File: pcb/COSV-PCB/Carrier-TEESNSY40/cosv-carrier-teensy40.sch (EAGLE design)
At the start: 25 parts, among them X1 057-006-1, X3 22-23-2031, X4 22-23-2031, X5 22-23-2031, X6 22-23-2031, X7 22-23-2031

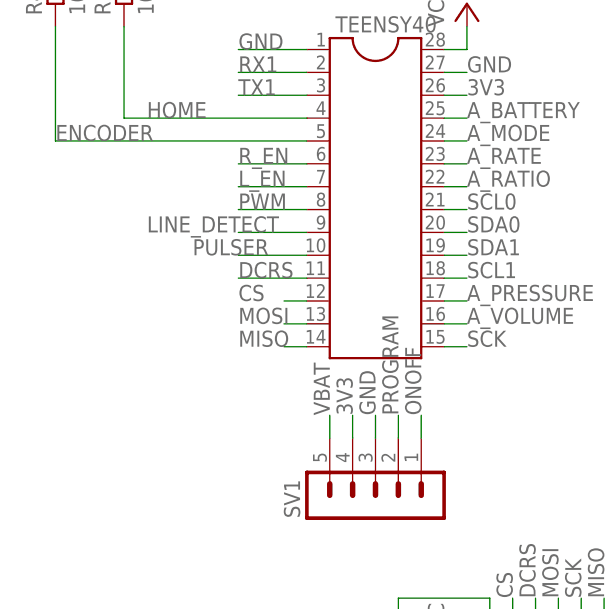
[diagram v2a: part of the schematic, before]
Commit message: Add Line Power Detect input and Watchdog Pulse output for alarm subsystem
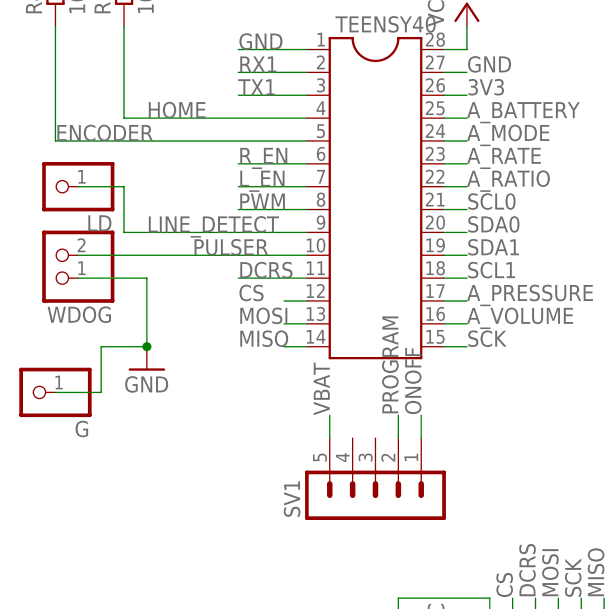
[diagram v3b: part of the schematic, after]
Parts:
- added G, LD: (no value), pinhead-2:PINHD-1X01_2.54-S
- added WDOG: (no value), pinhead:PINHD-1X2
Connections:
- net 3V3: no longer SV1.4
- net GND: now also G.1, WDOG.1; no longer SV1.3
- net LINE_DETECT: now also LD.1
- net PULSER: now also WDOG.2
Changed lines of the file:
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@@
 <grid distance="0.1" unitdist="inch" unit="inch" style="lines" multiple="1" display="no" altdistance="0.01" altunitdist="inch" altunit="inch"/>
 <layers>
-<layer number="1" name="Top" color="4" fill="1" visible="no" active="no"/>
-<layer number="16" name="Bottom" color="1" fill="1" visible="no" active="no"/>
-<layer number="17" name="Pads" color="2" fill="1" visible="no" active="no"/>
-<layer number="18" name="Vias" color="2" fill="1" visible="no" active="no"/>
-<layer number="19" name="Unrouted" color="6" fill="1" visible="no" active="no"/>
-<layer number="20" name="Dimension" color="15" fill="1" visible="no" active="no"/>
-<layer number="21" name="tPlace" color="7" fill="1" visible="no" active="no"/>
-<layer number="22" name="bPlace" color="7" fill="1" visible="no" active="no"/>
-<layer number="23" name="tOrigins" color="15" fill="1" visible="no" active="no"/>
-<layer number="24" name="bOrigins" color="15" fill="1" visible="no" active="no"/>
-<layer number="25" name="tNames" color="7" fill="1" visible="no" active="no"/>
-<layer number="26" name="bNames" color="7" fill="1" visible="no" active="no"/>
-<layer number="27" name="tValues" color="7" fill="1" visible="no" active="no"/>
-<layer number="28" name="bValues" color="7" fill="1" visible="no" active="no"/>
+<layer number="1" name="Top" color="4" fill="1" visible="yes" active="no"/>
+<layer number="16" name="Bottom" color="1" fill="1" visible="yes" active="no"/>
+<layer number="17" name="Pads" color="2" fill="1" visible="yes" active="no"/>
+<layer number="18" name="Vias" color="2" fill="1" visible="yes" active="no"/>
+<layer number="19" name="Unrouted" color="6" fill="1" visible="yes" active="no"/>
+<layer number="20" name="Dimension" color="15" fill="1" visible="yes" active="no"/>
+<layer number="21" name="tPlace" color="7" fill="1" visible="yes" active="no"/>
+<layer number="22" name="bPlace" color="7" fill="1" visible="yes" active="no"/>
+<layer number="23" name="tOrigins" color="15" fill="1" visible="yes" active="no"/>
+<layer number="24" name="bOrigins" color="15" fill="1" visible="yes" active="no"/>
+<layer number="25" name="tNames" color="7" fill="1" visible="yes" active="no"/>
+<layer number="26" name="bNames" color="7" fill="1" visible="yes" active="no"/>
+<layer number="27" name="tValues" color="7" fill="1" visible="yes" active="no"/>
+<layer number="28" name="bValues" color="7" fill="1" visible="yes" active="no"/>
 <layer number="29" name="tStop" color="7" fill="3" visible="no" active="no"/>
 <layer number="30" name="bStop" color="7" fill="6" visible="no" active="no"/>
@@
 <layer number="35" name="tGlue" color="7" fill="4" visible="no" active="no"/>
 <layer number="36" name="bGlue" color="7" fill="5" visible="no" active="no"/>
-<layer number="37" name="tTest" color="7" fill="1" visible="no" active="no"/>
-<layer number="38" name="bTest" color="7" fill="1" visible="no" active="no"/>
+<layer number="37" name="tTest" color="7" fill="1" visible="yes" active="no"/>
+<layer number="38" name="bTest" color="7" fill="1" visible="yes" active="no"/>
 <layer number="39" name="tKeepout" color="4" fill="11" visible="no" active="no"/>
 <layer number="40" name="bKeepout" color="1" fill="11" visible="no" active="no"/>
@@
 <layer number="44" name="Drills" color="7" fill="1" visible="no" active="no"/>
 <layer number="45" name="Holes" color="7" fill="1" visible="no" active="no"/>
-<layer number="46" name="Milling" color="3" fill="1" visible="no" active="no"/>
-<layer number="47" name="Measures" color="7" fill="1" visible="no" active="no"/>
-<layer number="48" name="Document" color="7" fill="1" visible="no" active="no"/>
-<layer number="49" name="Reference" color="7" fill="1" visible="no" active="no"/>
-<layer number="50" name="dxf" color="7" fill="1" visible="no" active="no"/>
-<layer number="51" name="tDocu" color="7" fill="1" visible="no" active="no"/>
-<layer number="52" name="bDocu" color="7" fill="1" visible="no" active="no"/>
-<layer number="53" name="tGND_GNDA" color="7" fill="9" visible="no" active="no"/>
-<layer number="54" name="bGND_GNDA" color="1" fill="9" visible="no" active="no"/>
-<layer number="56" name="wert" color="7" fill="1" visible="no" active="no"/>
-<layer number="57" name="tCAD" color="7" fill="1" visible="no" active="no"/>
-<layer number="58" name="bCAD" color="11" fill="1" visible="no" active="no"/>
-<layer number="59" name="tCarbon" color="7" fill="1" visible="no" active="no"/>
-<layer number="60" name="bCarbon" color="7" fill="1" visible="no" active="no"/>
+<layer number="46" name="Milling" color="3" fill="1" visible="yes" active="no"/>
+<layer number="47" name="Measures" color="7" fill="1" visible="yes" active="no"/>
+<layer number="48" name="Document" color="7" fill="1" visible="yes" active="no"/>
+<layer number="49" name="Reference" color="7" fill="1" visible="yes" active="no"/>
+<layer number="50" name="dxf" color="7" fill="1" visible="yes" active="no"/>
+<layer number="51" name="tDocu" color="7" fill="1" visible="yes" active="no"/>
+<layer number="52" name="bDocu" color="7" fill="1" visible="yes" active="no"/>
+<layer number="53" name="tGND_GNDA" color="7" fill="9" visible="yes" active="no"/>
+<layer number="54" name="bGND_GNDA" color="1" fill="9" visible="yes" active="no"/>
+<layer number="56" name="wert" color="7" fill="1" visible="yes" active="no"/>
+<layer number="57" name="tCAD" color="7" fill="1" visible="yes" active="no"/>
+<layer number="58" name="bCAD" color="11" fill="1" visible="yes" active="no"/>
+<layer number="59" name="tCarbon" color="7" fill="1" visible="yes" active="no"/>
+<layer number="60" name="bCarbon" color="7" fill="1" visible="yes" active="no"/>
 <layer number="88" name="SimResults" color="9" fill="1" visible="yes" active="yes"/>
 <layer number="89" name="SimProbes" color="9" fill="1" visible="yes" active="yes"/>
@@
 <part name="R4" library="resistor" deviceset="R-EU_" device="R0805" value="10K"/>
 <part name="3V3" library="jumper" deviceset="SJ" device=""/>
+<part name="WDOG" library="pinhead" deviceset="PINHD-1X2" device=""/>
+<part name="GND20" library="supply1" deviceset="GND" device=""/>
+<part name="LD" library="pinhead-2" deviceset="PINHD-1X01" device="_2.54-S"/>
+<part name="G" library="pinhead-2" deviceset="PINHD-1X01" device="_2.54-S"/>
 </parts>
 <sheets>
@@
 <instance part="R4" gate="G$1" x="-10.16" y="93.98" rot="R90"/>
 <instance part="3V3" gate="1" x="147.32" y="106.68"/>
+<instance part="WDOG" gate="G$1" x="-10.16" y="63.5" rot="R180"/>
+<instance part="GND20" gate="1" x="0" y="50.8"/>
+<instance part="LD" gate="A" x="-10.16" y="71.12" rot="R180"/>
+<instance part="G" gate="A" x="-12.7" y="48.26" rot="R180"/>
 </instances>
 <busses>
@@
 </segment>
 <segment>
-<pinref part="SV1" gate="G$1" pin="3"/>
-<wire x1="25.4" y1="43.18" x2="25.4" y2="45.72" width="0.1524" layer="91"/>
-<label x="25.4" y="45.72" size="1.778" layer="95" rot="R90"/>
-</segment>
-<segment>
 <pinref part="SV5" gate="G$1" pin="1"/>
 <pinref part="GND2" gate="1" pin="GND"/>
@@
 <wire x1="63.5" y1="63.5" x2="55.88" y2="63.5" width="0.1524" layer="91"/>
 <wire x1="55.88" y1="63.5" x2="55.88" y2="58.42" width="0.1524" layer="91"/>
+</segment>
+<segment>
+<pinref part="GND20" gate="1" pin="GND"/>
+<wire x1="0" y1="53.34" x2="0" y2="60.96" width="0.1524" layer="91"/>
+<pinref part="WDOG" gate="G$1" pin="1"/>
+<wire x1="0" y1="60.96" x2="-7.62" y2="60.96" width="0.1524" layer="91"/>
+<pinref part="G" gate="A" pin="1"/>
+<wire x1="-10.16" y1="48.26" x2="-5.08" y2="48.26" width="0.1524" layer="91"/>
+<wire x1="-5.08" y1="48.26" x2="-5.08" y2="53.34" width="0.1524" layer="91"/>
+<wire x1="-5.08" y1="53.34" x2="0" y2="53.34" width="0.1524" layer="91"/>
+<junction x="0" y="53.34"/>
 </segment>
 </net>
@@
 <segment>
 <pinref part="TEENSY40" gate="G$1" pin="9"/>
-<wire x1="17.78" y1="66.04" x2="10.16" y2="66.04" width="0.1524" layer="91"/>
 <label x="0" y="66.04" size="1.778" layer="95"/>
+<wire x1="17.78" y1="66.04" x2="-2.54" y2="66.04" width="0.1524" layer="91"/>
+<wire x1="-2.54" y1="66.04" x2="-2.54" y2="71.12" width="0.1524" layer="91"/>
+<pinref part="LD" gate="A" pin="1"/>
+<wire x1="-2.54" y1="71.12" x2="-7.62" y2="71.12" width="0.1524" layer="91"/>
 </segment>
 <segment>
@@
 <segment>
 <pinref part="TEENSY40" gate="G$1" pin="10"/>
-<wire x1="17.78" y1="63.5" x2="10.16" y2="63.5" width="0.1524" layer="91"/>
 <label x="5.08" y="63.5" size="1.778" layer="95"/>
+<pinref part="WDOG" gate="G$1" pin="2"/>
+<wire x1="17.78" y1="63.5" x2="-7.62" y2="63.5" width="0.1524" layer="91"/>
 </segment>
 <segment>
@@
 </segment>
 <segment>
-<pinref part="SV1" gate="G$1" pin="4"/>
-<wire x1="22.86" y1="43.18" x2="22.86" y2="45.72" width="0.1524" layer="91"/>
-<label x="22.86" y="45.72" size="1.778" layer="95" rot="R90"/>
-</segment>
-<segment>

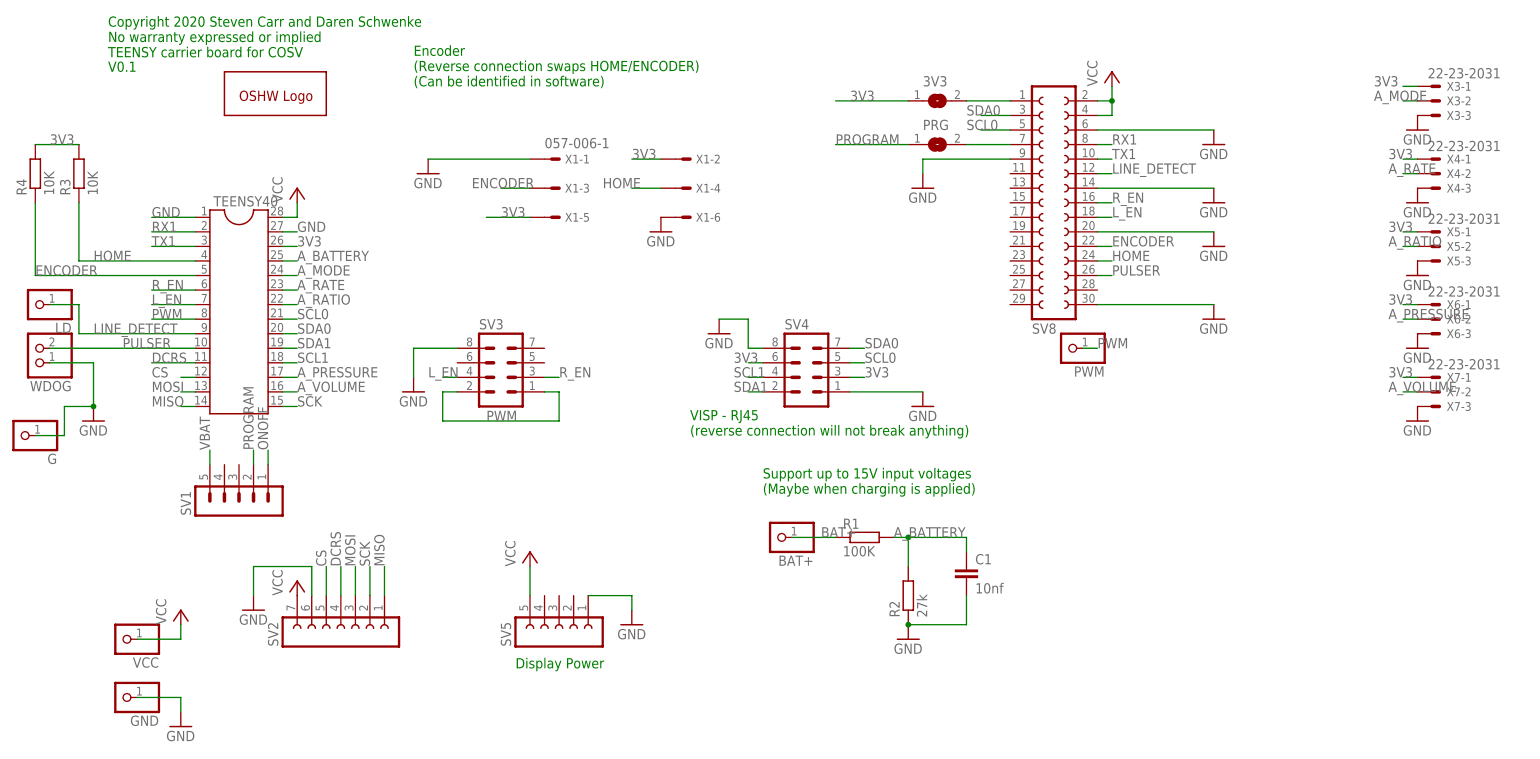
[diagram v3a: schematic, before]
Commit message: New "millable" Carrier board for use with rPI3+ on COSV
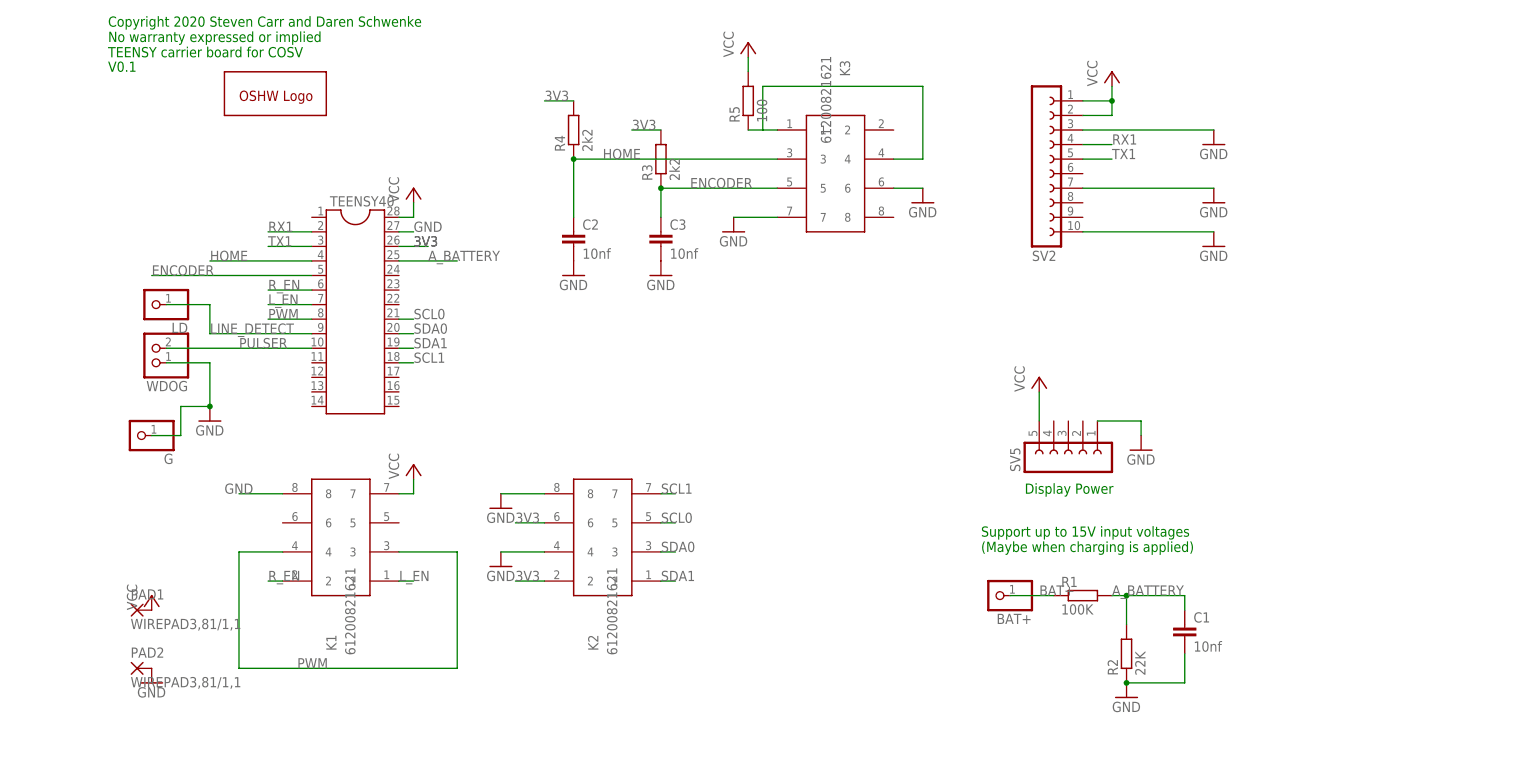
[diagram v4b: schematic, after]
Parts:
- removed 3V3, PRG: (no value), jumper:SJ
- removed GND, PWM, VCC: (no value), pinhead-2:PINHD-1X01_2.54-S
- removed SV1: (no value), con-lstb:MA05-1
- removed SV3, SV4: (no value), con-lstb:MA04-2
- removed SV8: (no value), con-lsta:FE15-2
- removed X1: 057-006-1, con-panduit:057-006-1
- removed X3, X4, X5, X6, X7: 22-23-2031, con-molex:22-23-2031
- added C2, C3: 10nf, rcl:C-EUC1206
- added K1, K2, K3: 61200821621, Wuerth_Elektronik_eiCan_05_Box_Header_IDC_Connectors_1_2:61200821621
- added PAD1, PAD2: WIREPAD3,81/1,1, wirepad:WIREPAD3,81/1,1
- added R5: 100, resistor:R-EU_R1206
- C1: device rcl:C-EUC0805 -> rcl:C-EUC1206
- R1: device resistor:R-EU_R0805 -> resistor:R-EU_R1206
- R2: value 27k -> 22K; device resistor:R-EU_R0805 -> resistor:R-EU_R1206
- R3, R4: value 10K -> 2k2; device resistor:R-EU_R0805 -> resistor:R-EU_R1206
- SV2: device con-lsta:FE07-1 -> con-lsta:FE10-1
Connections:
- removed net A_MODE: TEENSY40.24, X3-2.S
- removed net A_PRESSURE: TEENSY40.17, X6-2.S
- removed net A_RATE: TEENSY40.23, X4-2.S
- removed net A_RATIO: TEENSY40.22, X5-2.S
- removed net A_VOLUME: TEENSY40.16, X7-2.S
- removed net CS: SV2.5, TEENSY40.12
- removed net DCRS: SV2.4, TEENSY40.11
- removed net MISO: SV2.1, TEENSY40.14
- removed net MOSI: SV2.3, TEENSY40.13
- removed net N$3: 3V3.2, SV8.1
- removed net ONOFF: SV1.1
- removed net PROGRAM: PRG.1, SV1.2
- removed net SCK: SV2.2, TEENSY40.15
- removed net VBAT: SV1.5
- net 3V3: now also K2.2, K2.6; no longer 3V3.1, SV4.3, SV4.6, X1-2.S, X1-5.S, X3-1.S, X4-1.S, X5-1.S, X6-1.S, X7-1.S
- net ENCODER: now also C3.1, K3.5, R3.1; no longer R4.1, SV8.22, X1-3.S
- net GND: now also C2.2, C3.2, K1.8, K2.4, K2.8, K3.6, K3.7, PAD2.P, SV2.10, SV2.3, SV2.7; no longer GND.1, SV2.6, SV3.8, SV4.1, SV4.8, SV8.14, SV8.20, SV8.30, SV8.6, SV8.9, TEENSY40.1, X1-1.S, X1-6.S, X3-3.S, X4-3.S, X5-3.S, X6-3.S, X7-3.S
- net HOME: now also C2.1, K3.3, R4.1; no longer R3.1, SV8.24, X1-4.S
- net LINE_DETECT: no longer SV8.12
- net L_EN: now also K1.1; no longer SV3.4, SV8.18
- net N$1: now also K3.1, K3.4, R5.1; no longer PRG.2, SV8.7
- net PULSER: no longer SV8.26
- net PWM: now also K1.3, K1.4; no longer PWM.1, SV3.1, SV3.2
- net RX1: now also SV2.4; no longer SV8.8
- net R_EN: now also K1.2; no longer SV3.3, SV8.16
- net SCL0: now also K2.5; no longer SV4.5, SV8.5
- net SCL1: now also K2.7; no longer SV4.4
- net SDA0: now also K2.3; no longer SV4.7, SV8.3
- net SDA1: now also K2.1; no longer SV4.2
- net TX1: now also SV2.5; no longer SV8.10
- net VCC: now also K1.7, PAD1.P, R5.2, SV2.1, SV2.2; no longer SV2.7, SV8.2, SV8.4, VCC.1
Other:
- note removed: "Encoder (Reverse connection swaps HOME/ENCODER) (Can be identified in software)"
- note removed: "VISP - RJ45 (reverse connection will not break anything)"
- moved on the sheet: BAT+, C1, G, LD, R1, R2, R3, R4, SV5, TEENSY40, WDOG
